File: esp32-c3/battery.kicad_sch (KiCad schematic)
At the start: 9 parts, among them J3 Conn_01x02_Pin, U6 TPS5430DDA

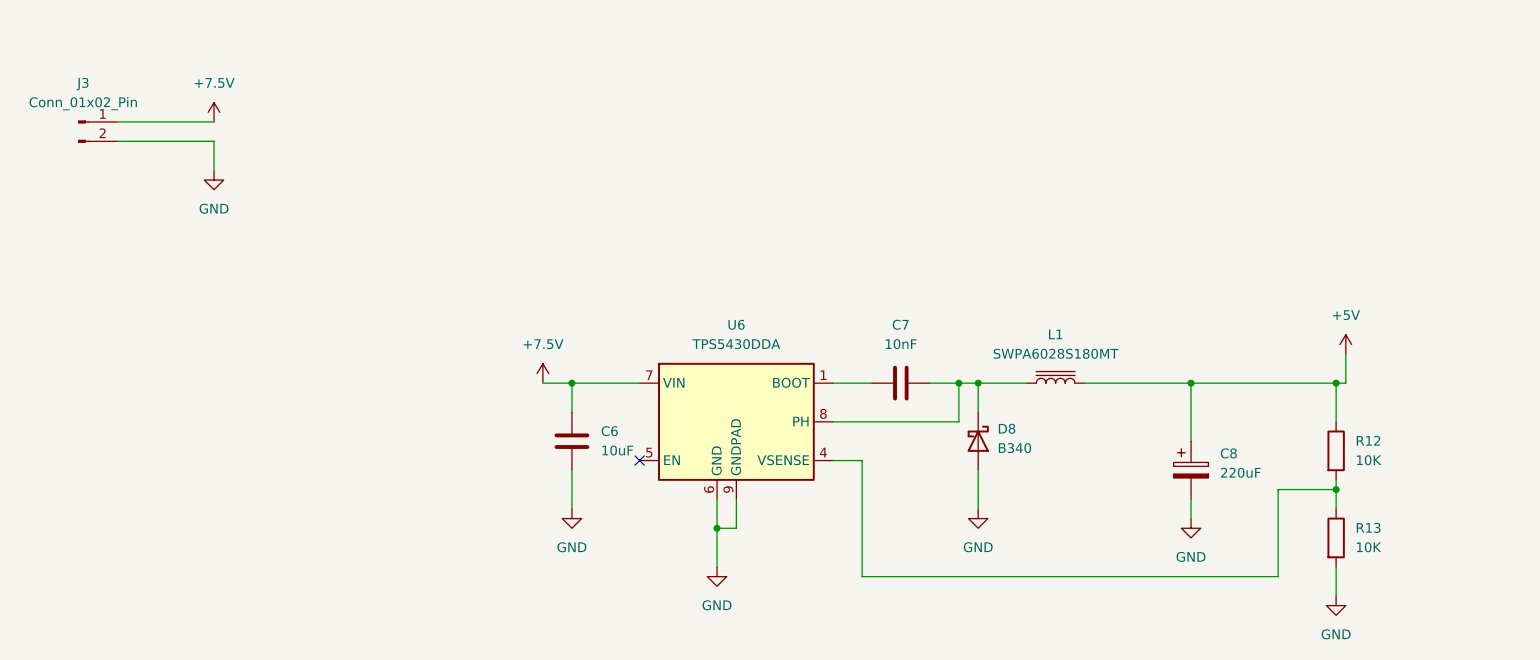
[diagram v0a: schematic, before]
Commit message: Fix Battery power and USB/UART connection, move vent around to accomodate enclosure
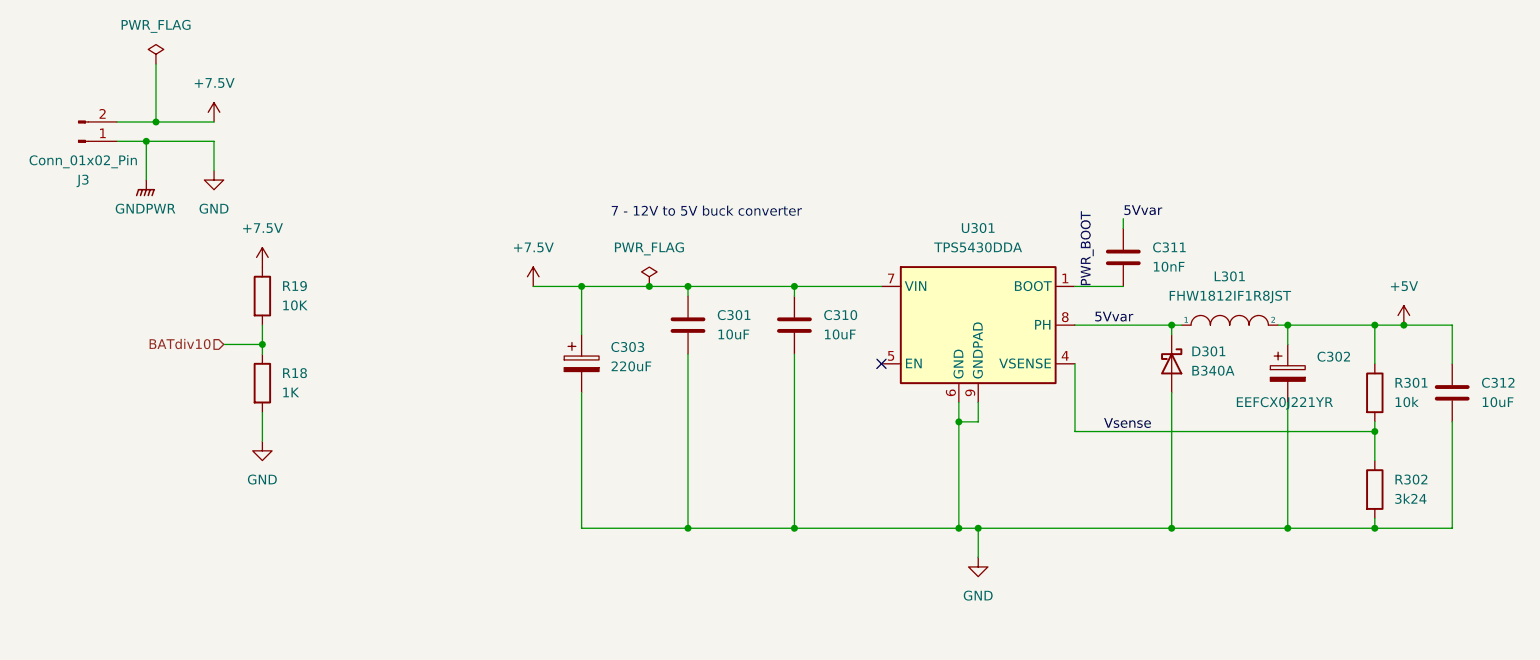
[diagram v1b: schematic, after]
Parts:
- removed C6: 10uF, Capacitor_SMD:C_0805_2012Metric, symbol Device:C
- removed C7: 10nF, Capacitor_SMD:C_0402_1005Metric, symbol Device:C
- removed C8: 220uF, Capacitor_Tantalum_SMD:CP_EIA-7343-43_Kemet-X, symbol Device:C_Polarized
- removed D8: B340, Diode_SMD:D_SMC, symbol Diode:B340
- removed L1: SWPA6028S180MT, inductor:Inductor_6x6mm, symbol Device:L_Iron
- removed R12, R13: 10K, Resistor_SMD:R_0402_1005Metric, symbol Device:R
- removed U6: TPS5430DDA, Package_SO:TI_SO-PowerPAD-8_ThermalVias, symbol Regulator_Switching:TPS5430DDA
- added C301, C310, C312: 10uF, Capacitor_SMD:C_1206_3216Metric, symbol Device:C
- added C302: EEFCX0J221YR, local:CP_SMD_4.3x7.3mm, symbol Device:C_Polarized
- added C303: 220uF, Capacitor_Tantalum_SMD:CP_EIA-7343-31_Kemet-D, symbol Device:C_Polarized
- added C311: 10nF, Capacitor_SMD:C_0402_1005Metric, symbol Device:C
- added D301: B340A, Diode_SMD:D_SMA, symbol Device:D_Schottky
- added L301: FHW1812IF1R8JST, Inductor_SMD:L_1812_4532Metric, symbol pspice:INDUCTOR
- added R18: 1K, Resistor_SMD:R_0402_1005Metric, symbol Device:R
- added R19: 10K, Resistor_SMD:R_0402_1005Metric, symbol Device:R
- added R301: 10k, Resistor_SMD:R_0402_1005Metric, symbol Device:R
- added R302: 3k24, Resistor_SMD:R_0402_1005Metric, symbol Device:R
- added U301: TPS5430DDA, Package_SO:TI_SO-PowerPAD-8_ThermalVias, symbol Regulator_Switching:TPS5430DDA
- J3: footprint Connector_JST:JST_XH_S2B-XH-A_1x02_P2.50mm_Horizontal -> Connector_AMASS:AMASS_XT30PW-M_1x02_P2.50mm_Horizontal
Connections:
- net +5V: now also C302.1, C312.1, L301.2, R301.1
- net +7.5V: now also J3.2 (Pin_2), C301.1, C303.1, C310.1, R19.1, U301.7 (VIN); no longer J3.1 (Pin_1)
- net GND: now also J3.1 (Pin_1), C301.2, C302.2, C303.2, C310.2, C312.2, D301.2 (A), R18.2, R302.2, U301.6 (GND), U301.9 (GNDPAD); no longer J3.2 (Pin_2)
- new net 5Vvar: C311.2, D301.1 (K), L301.1, U301.8 (PH)
- new net BATdiv10: R18.1, R19.2
- new net PWR_BOOT: C311.1, U301.1 (BOOT)
- new net Vsense: R301.2, R302.1, U301.4 (VSENSE)
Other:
- note added: "7 - 12V to 5V buck converter"
